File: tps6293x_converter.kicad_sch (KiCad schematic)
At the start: 11 parts, among them U2 TPS62933

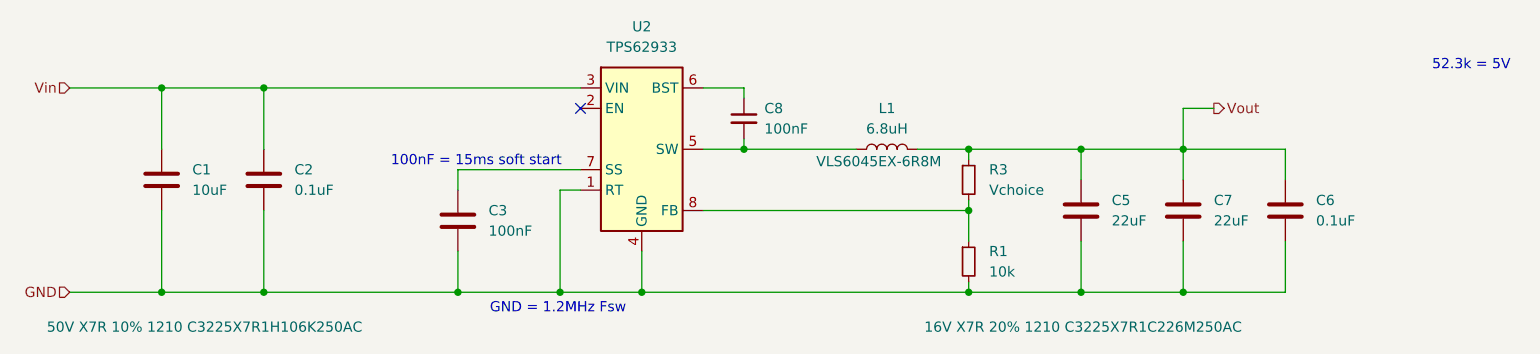
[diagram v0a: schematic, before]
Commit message: sch: assign correct footprint
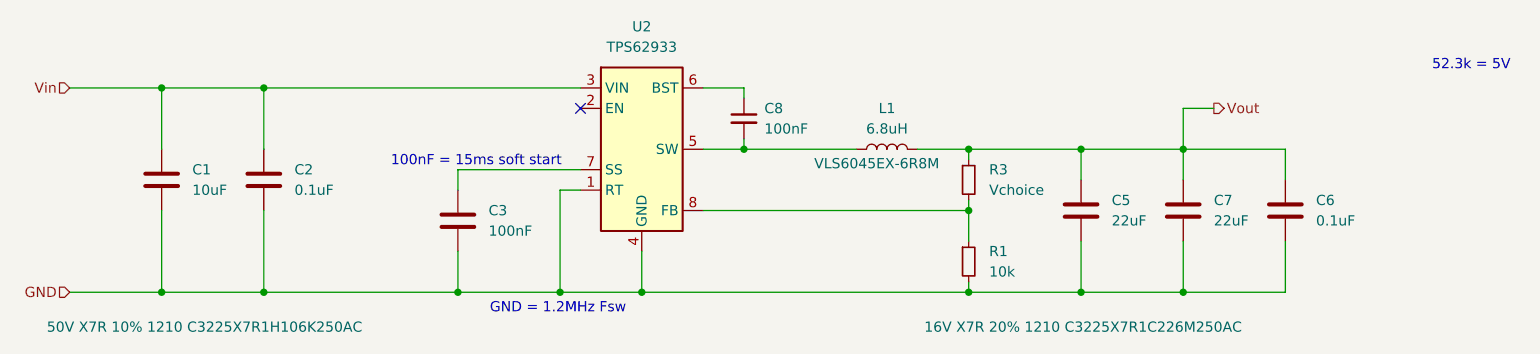
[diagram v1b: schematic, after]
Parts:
- L1: footprint Inductor_SMD:L_TDK_VLS6045EX_VLS6045AF -> Inductor:L_TDK_VLS6045EX_VLS6045AF
- U2: footprint Package_TO_SOT_SMD:SOT-583-8 -> SOT:SOT-583-8
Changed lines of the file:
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@@
 			)
 		)
-		(property "Footprint" "Inductor_SMD:L_TDK_VLS6045EX_VLS6045AF"
+		(property "Footprint" "Inductor:L_TDK_VLS6045EX_VLS6045AF"
 			(at 127 33.02 0)
 			(effects
@@
 		)
 		(property "Description" "VLS6045EX-6R8M"
-			(at 125.984 34.544 90)
+			(at 125.73 34.798 90)
 			(effects
 				(font
@@
 			)
 		)
-		(property "Footprint" "Package_TO_SOT_SMD:SOT-583-8"
+		(property "Footprint" "SOT:SOT-583-8"
 			(at 96.52 58.42 0)
 			(effects

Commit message: pcb: first draft
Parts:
- R1: renamed from R3; now not fitted
- renumbered C8 to C4, C6 to C5, C5 to C6, R1 to R2, U2 to U1
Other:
- moved on the sheet: C5, C6, C7

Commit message: pcb: change DNI footprint
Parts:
- R1: footprint Resistor_SMD:R_0603_1608Metric -> SMD:0603_1608Metric_DNI_NoPaste
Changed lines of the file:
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@@
 			)
 		)
-		(property "Footprint" "Resistor_SMD:R_0603_1608Metric"
+		(property "Footprint" "SMD:0603_1608Metric_DNI_NoPaste"
 			(at 137.16 36.83 0)
 			(effects

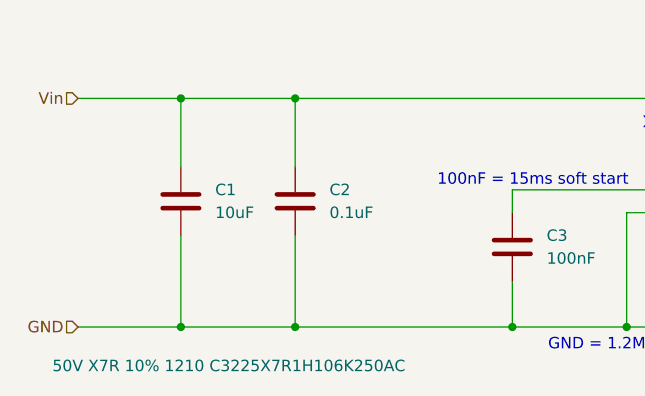
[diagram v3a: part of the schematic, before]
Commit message: sch: change input cap value
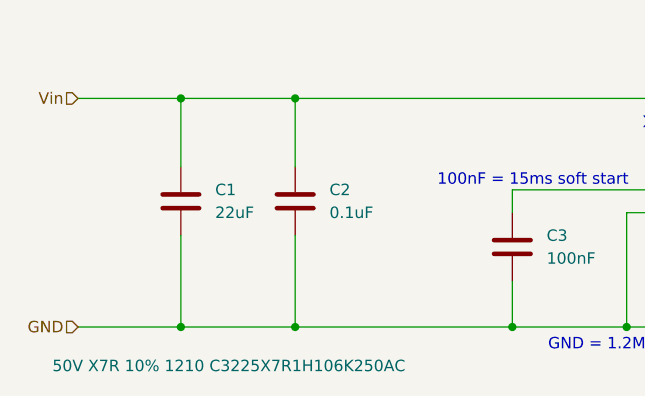
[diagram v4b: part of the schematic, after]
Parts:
- C1: value 10uF -> 22uF
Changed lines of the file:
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@@
 			)
 		)
-		(property "Value" "10uF"
+		(property "Value" "22uF"
 			(at 40.64 38.0999 0)
 			(effects
